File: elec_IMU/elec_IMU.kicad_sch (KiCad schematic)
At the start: 22 parts, among them J1 JST SH, J2 JST SH, U1 BMI088

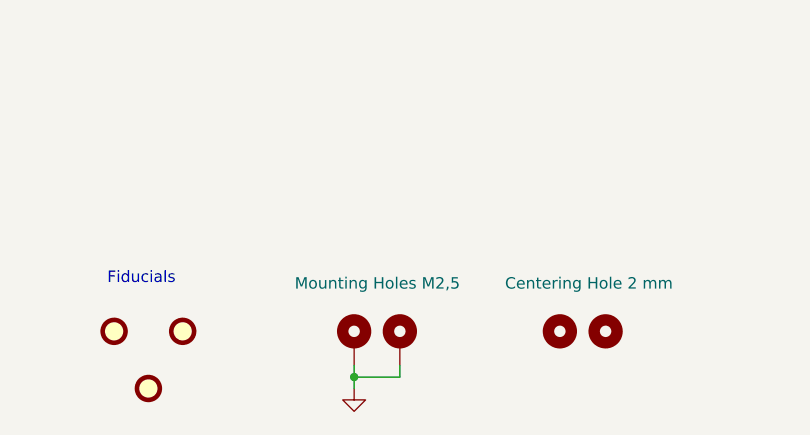
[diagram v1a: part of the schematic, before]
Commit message: [update] Mechanical adaptations.
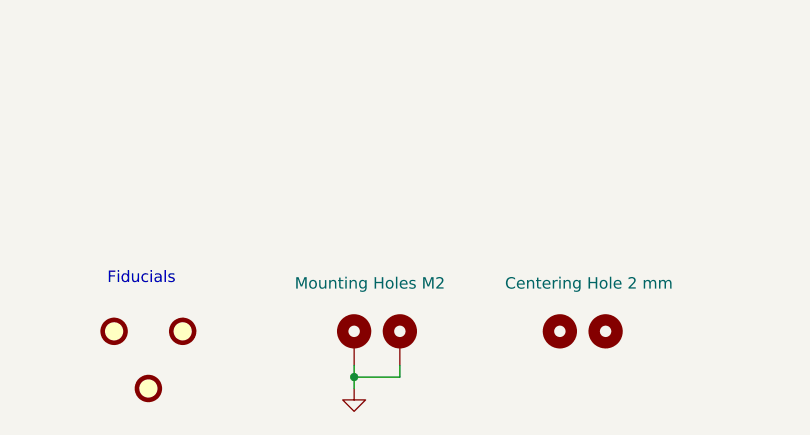
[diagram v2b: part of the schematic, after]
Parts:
- H4: value Mounting Holes M2,5 -> Mounting Holes M2; footprint MountingHole:MountingHole_2.7mm_M2.5_ISO7380_Pad_TopBottom -> MountingHole:MountingHole_2.2mm_M2_ISO7380_Pad_TopBottom
- H5: value MountingHole_Pad -> Mounting Holes M2; footprint MountingHole:MountingHole_2.7mm_M2.5_ISO7380_Pad_TopBottom -> MountingHole:MountingHole_2.2mm_M2_ISO7380_Pad_TopBottom
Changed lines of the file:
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@@
 			)
 		)
-		(property "Value" "MountingHole_Pad"
+		(property "Value" "Mounting Holes M2"
 			(at 125.73 166.37 0)
 			(effects
@@
 			)
 		)
-		(property "Footprint" "MountingHole:MountingHole_2.7mm_M2.5_ISO7380_Pad_TopBottom"
+		(property "Footprint" "MountingHole:MountingHole_2.2mm_M2_ISO7380_Pad_TopBottom"
 			(at 119.38 172.72 0)
 			(effects
@@
 		)
 		(instances
-			(project "elec_forcathon"
+			(project "elec_IMU"
 				(path "/bc05f5da-608c-4912-90e4-36b13d989976"
 					(reference "H1")
@@
 		)
 		(instances
-			(project "elec_forcathon"
+			(project "elec_IMU"
 				(path "/bc05f5da-608c-4912-90e4-36b13d989976"
 					(reference "FID3")
@@
 			)
 		)
-		(property "Value" "Mounting Holes M2,5"
+		(property "Value" "Mounting Holes M2"
 			(at 107.696 166.116 0)
 			(effects
@@
 			)
 		)
-		(property "Footprint" "MountingHole:MountingHole_2.7mm_M2.5_ISO7380_Pad_TopBottom"
+		(property "Footprint" "MountingHole:MountingHole_2.2mm_M2_ISO7380_Pad_TopBottom"
 			(at 114.3 172.72 0)
 			(effects
@@
 		)
 		(instances
-			(project "elec_forcathon"
+			(project "elec_IMU"
 				(path "/bc05f5da-608c-4912-90e4-36b13d989976"
 					(reference "FID1")
@@
 		)
 		(instances
-			(project "elec_angle_sensor"
+			(project "elec_IMU"
 				(path "/bc05f5da-608c-4912-90e4-36b13d989976"
 					(reference "#PWR01")
@@
 		)
 		(instances
-			(project ""
+			(project "elec_IMU"
 				(path "/bc05f5da-608c-4912-90e4-36b13d989976"
 					(reference "#PWR02")
@@
 		)
 		(instances
-			(project "elec_angle_sensor"
+			(project "elec_IMU"
 				(path "/bc05f5da-608c-4912-90e4-36b13d989976"
 					(reference "G1")
@@
 		)
 		(instances
-			(project "elec_forcathon"
+			(project "elec_IMU"
 				(path "/bc05f5da-608c-4912-90e4-36b13d989976"
 					(reference "FID2")
@@
 		)
 		(instances
-			(project ""
+			(project "elec_IMU"
 				(path "/bc05f5da-608c-4912-90e4-36b13d989976"
 					(reference "#FLG02")
@@
 		)
 		(instances
-			(project ""
+			(project "elec_IMU"
 				(path "/bc05f5da-608c-4912-90e4-36b13d989976"
 					(reference "#FLG01")
@@
 		)
 		(instances
-			(project "elec_angle_sensor"
+			(project "elec_IMU"
 				(path "/bc05f5da-608c-4912-90e4-36b13d989976"
 					(reference "D1")
@@
 		)
 		(instances
-			(project "elec_forcathon"
+			(project "elec_IMU"
 				(path "/bc05f5da-608c-4912-90e4-36b13d989976"
 					(reference "H3")
@@
 		)
 		(instances
-			(project ""
+			(project "elec_IMU"
 				(path "/bc05f5da-608c-4912-90e4-36b13d989976"
 					(reference "H2")
@@
 		)
 		(instances
-			(project "elec_angle_sensor"
+			(project "elec_IMU"
 				(path "/bc05f5da-608c-4912-90e4-36b13d989976"
 					(reference "#PWR03")
@@
 		)
 		(instances
-			(project "elec_angle_sensor"
+			(project "elec_IMU"
 				(path "/bc05f5da-608c-4912-90e4-36b13d989976"
 					(reference "J1")
